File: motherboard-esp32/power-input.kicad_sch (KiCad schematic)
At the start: 8 parts, among them J1 XT60, Q1 MCU60P04-TP, Q2 MCU60P04-TP, SW1 RA1H1C112R

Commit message: boards
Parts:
- removed SW1: RA1H1C112R, bots:SW_RA1H1C112R, symbol bots:RA1H1C112R
- added J2: XT60, bots:XT60_12-14AWG_POWER, symbol bio-robot:XT-60
- added J3: JST_2P_XH, bots:JST_B2B-XH-A_LF__SN_, symbol bio-robot:JST_XH-2
- D1: value SMAZ12-13F -> SMAZ6V8; footprint bots:D_SMB -> bots:D_SMA; symbol bots:D_ZENER_SMAZ12-13F -> bio-robot:D_ZENER_SMAZ6V8; JLC (none) -> DO-214AC(SMA); LCSC C260227 -> C2988335; MPN SMAZ12-13F -> SMAZ6V8; Manufacturer Micro Commercial Co -> EIC Semicon C; Price 0.63 -> 0.1464
- F1: value 0501015.WR1 -> 0437005.WR; symbol bots:Fuse_0501015.WR1 -> bio-robot:Fuse_Littelfuse5A; LCSC C410346 -> C99541; MPN 0501015.WR1 -> 0437005.WR; Price 0.0992 -> 0.1509
- J1: symbol bots:XT-60 -> bio-robot:XT-60
- Q1, Q2: value MCU60P04-TP -> DOD4185; symbol bots:MCU60P04-TP -> bio-robot:Q_Pch40V45A; LCSC C130101 -> C41430591; MPN (none) -> DOD4185
- R1, R2: symbol bots:R_100k -> bio-robot:R_100k
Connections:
- net GND: now also J2.1, J3.2
- net SW: now also J3.1
- net VBAT: now also J2.2
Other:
- note added: "3 cell battery -> 12.6V max, 10.2V min. parallel for modularity"

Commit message: proof of concept
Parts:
- removed F1: 0437005.WR, bots:Fuse_1206_3216Metric, symbol bio-robot:Fuse_Littelfuse5A
- removed J1, J2: XT60, bots:XT60_12-14AWG_POWER, symbol bio-robot:XT-60
- added BT1, BT2, BT3, BT4, BT5, BT6: Keystone_254_BatteryClip_Holder, bio-robot:BAT_254_18650_Holder, symbol bio-robot:Keystone_254_BatteryClip_Holder
- added F2: 0501010.WR1, bio-robot:Fuse_1206_3216Metric, symbol bio-robot:Fuse_0501010.WR1
- D1: footprint bots:D_SMA -> bio-robot:D_SMA
- J3: footprint bots:JST_B2B-XH-A_LF__SN_ -> bio-robot:JST_B2B-XH-A_LF__SN_
- Q1, Q2: footprint bots:DPAK-3_ONS -> bio-robot:DPAK-3_ONS
- R1, R2: footprint bots:R_0603_1608Metric -> bio-robot:R_0603_1608Metric
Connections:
- net FUSE_VCC: now also F2.2
- net GND: now also BT3.P-, BT6.P-
- net VBAT: now also BT1.P+, BT4.P+, F2.1
- new net: BT2.P-, BT3.P+
- new net: BT4.P-, BT5.P+
- new net: BT5.P-, BT6.P+
- new net: BT1.P-, BT2.P+
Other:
- note added: "3 cell battery -> 12.6V max, 10.2V min. parallel for modularity board contact 18650 holders can generally only go up to 3-5A max so 2 in parallel allow up to 10A continous."
- note removed: "3 cell battery -> 12.6V max, 10.2V min. parallel for modularity"

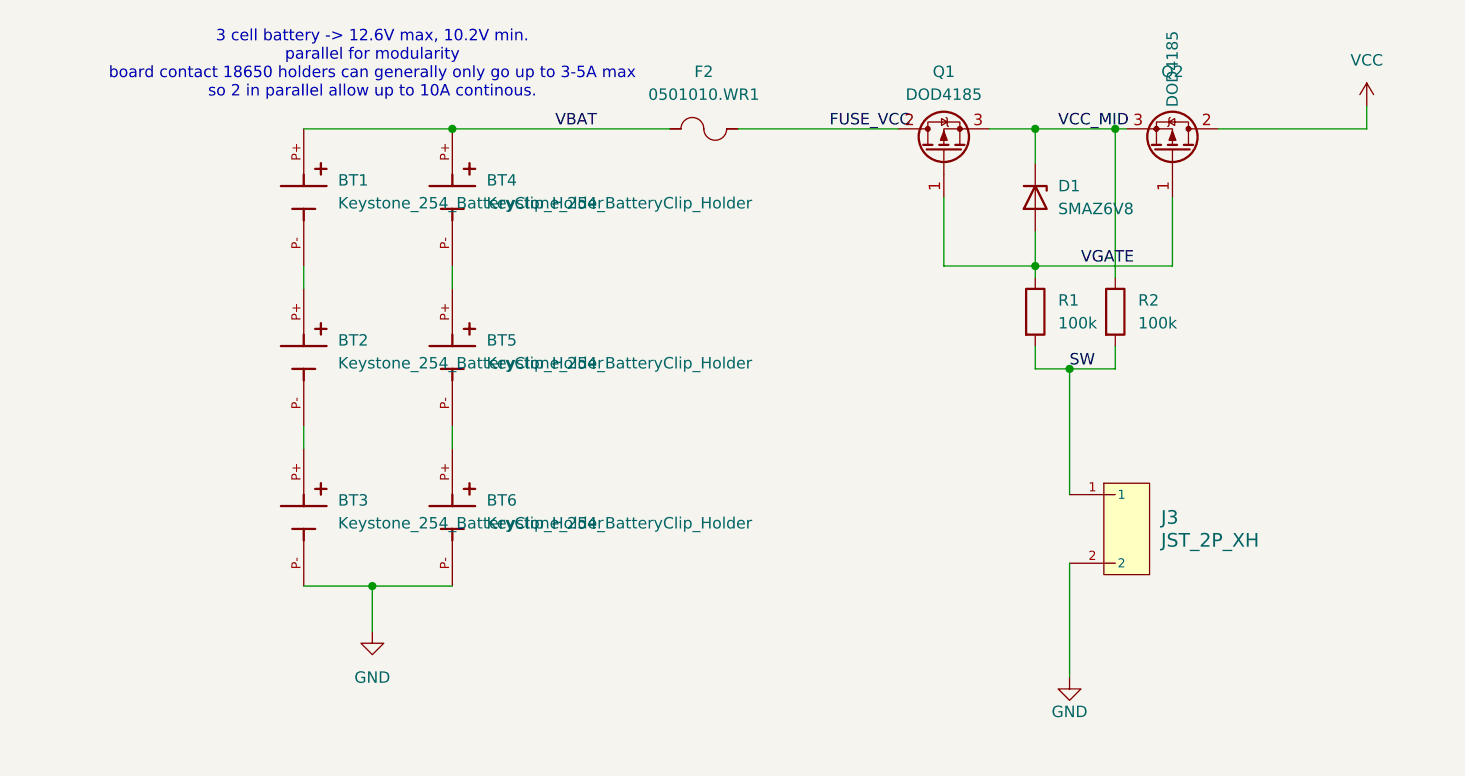
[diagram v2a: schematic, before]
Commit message: split into two boards for dc/dc converter
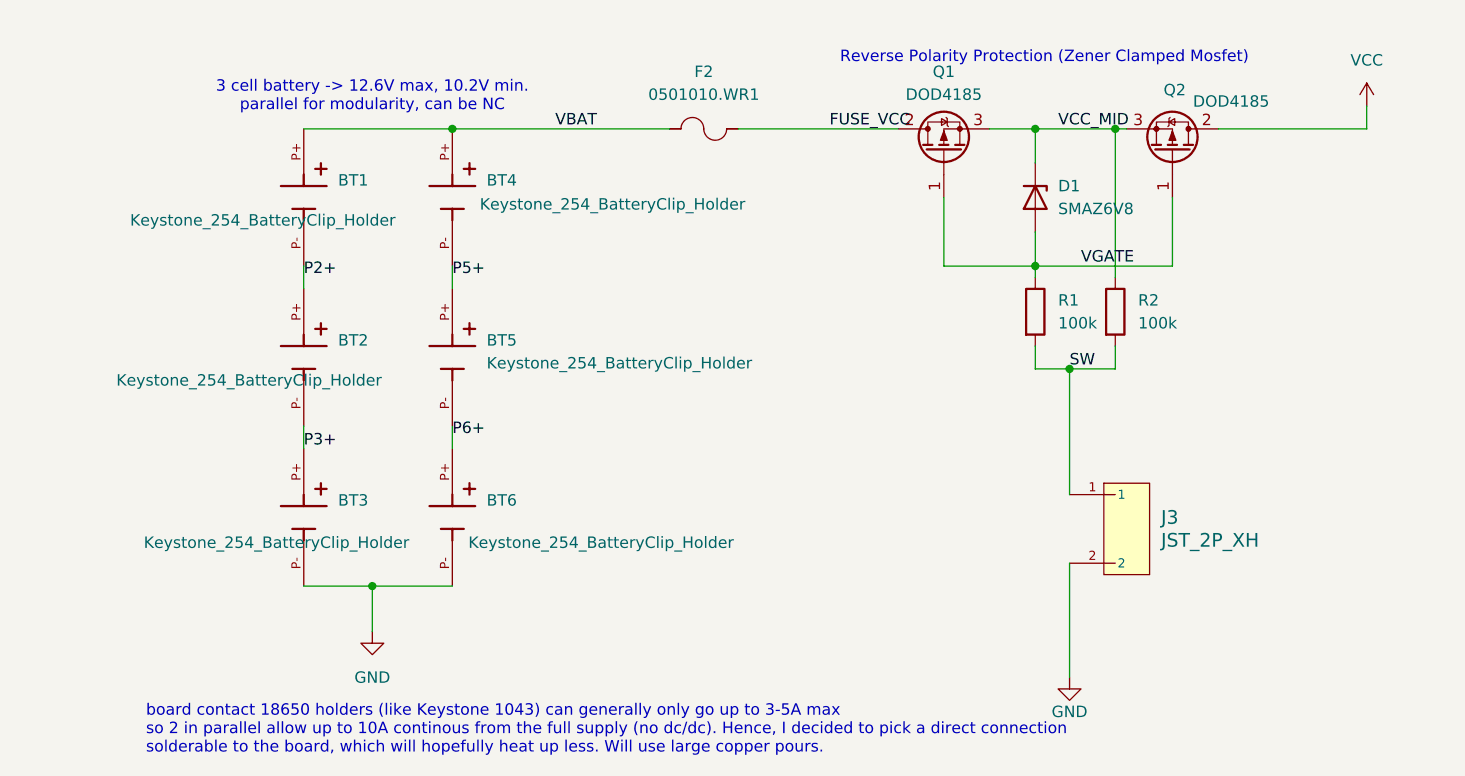
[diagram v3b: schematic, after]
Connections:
- net P3+: now reaches BT2.P-, BT3.P+
- net P5+: now reaches BT4.P-, BT5.P+
- net P6+: now reaches BT5.P-, BT6.P+
- net P2+: now reaches BT1.P-, BT2.P+
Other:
- note added: "3 cell battery -> 12.6V max, 10.2V min. parallel for modularity, can be NC"
- note added: "Reverse Polarity Protection (Zener Clamped Mosfet)"
- note added: "board contact 18650 holders (like Keystone 1043) can generally only go up to 3-5A max so 2 in parallel allow up to 10A continous from the full supply (no dc/dc). Hence, I decided to pick a direct connection solderable to the board, which will hopefully heat up less. Will use large copper pours."
- note removed: "3 cell battery -> 12.6V max, 10.2V min. parallel for modularity board contact 18650 holders can generally only go up to 3-5A max so 2 in parallel allow up to 10A continous."

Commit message: update
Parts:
- removed BT1, BT2, BT3, BT4, BT5, BT6: Keystone_254_BatteryClip_Holder, bio-robot:BAT_254_18650_Holder, symbol bio-robot:Keystone_254_BatteryClip_Holder
- added BT8: Keystone_1048P_DualBatteryHolder, bio-robot:BAT_1048P, symbol bio-robot:Keystone_1048P_DualBatteryHolder
- added D2: SMAZ3V6, bots:D_SMA, symbol bio-robot:D_ZENER_SMAZ3V6
- added F1: 0437005.WR, bio-robot:Fuse_1206_3216Metric, symbol bio-robot:Fuse_0437005.WR
- added J4: JST_2P_XH, bio-robot:JST_B2B-XH-A_LF__SN_, symbol bio-robot:JST_XH-2
- added J7: XT60, bio-robot:AMASS_XT60PW-M, symbol bio-robot:XT-60-RA
- added Q3, Q4: DOD4185, bio-robot:DPAK-3_ONS, symbol bio-robot:Q_Pch40V45A
- added R3, R4: 100k, bio-robot:R_0603_1608Metric, symbol bio-robot:R_100k
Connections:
- net GND: now also BT8.N2, J4.2; no longer J3.2
- net VBAT: now also J7.2
- new net +BATT: Q4.2 (D)
- new net BAT5V_MID: D2.1 (K), Q3.3 (S), Q4.3 (S), R4.1
- new net FUSE_BAT5V: F1.2, Q3.2 (D)
- new net GNDPWR: J3.2, J7.1
- new net SW2: J4.1, R3.2, R4.2
- new net VBAT5V: BT8.P1, F1.1
- new net VBAT5V_P2: BT8.N1, BT8.P2
- new net VGATE_2: D2.2 (A), Q3.1 (G), Q4.1 (G), R3.1
- no-connect marks 0 -> 1
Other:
- note added: "3 cell battery -> 12.6V max, 10.2V min."
- note removed: "3 cell battery -> 12.6V max, 10.2V min. parallel for modularity, can be NC"
- moved on the sheet: D1, F2, J3, Q1, Q2, R1, R2

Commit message: update
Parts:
- D1: footprint bio-robot:D_SMA -> bots:D_SMA
- J3, J4: footprint bio-robot:JST_B2B-XH-A_LF__SN_ -> bots:JST_B2B-XH-A_LF__SN_
- Q1, Q2, Q3, Q4: footprint bio-robot:DPAK-3_ONS -> bots:DPAK-3_ONS
- R1, R2, R3, R4: footprint bio-robot:R_0603_1608Metric -> bots:R_0603_1608Metric
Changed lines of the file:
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@@
 			)
 		)
-		(property "Footprint" "bio-robot:JST_B2B-XH-A_LF__SN_"
+		(property "Footprint" "bots:JST_B2B-XH-A_LF__SN_"
 			(at 116.84 107.95 0)
 			(hide yes)
@@
 			)
 		)
-		(property "Footprint" "bio-robot:R_0603_1608Metric"
+		(property "Footprint" "bots:R_0603_1608Metric"
 			(at 104.902 111.76 90)
 			(hide yes)
@@
 			)
 		)
-		(property "Footprint" "bio-robot:DPAK-3_ONS"
+		(property "Footprint" "bots:DPAK-3_ONS"
 			(at 111.125 89.027 0)
 			(hide yes)
@@
 			)
 		)
-		(property "Footprint" "bio-robot:R_0603_1608Metric"
+		(property "Footprint" "bots:R_0603_1608Metric"
 			(at 121.412 49.53 90)
 			(hide yes)
@@
 			)
 		)
-		(property "Footprint" "bio-robot:D_SMA"
+		(property "Footprint" "bots:D_SMA"
 			(at 123.19 36.83 0)
 			(hide yes)
@@
 			)
 		)
-		(property "Footprint" "bio-robot:R_0603_1608Metric"
+		(property "Footprint" "bots:R_0603_1608Metric"
 			(at 96.012 111.76 90)
 			(hide yes)
@@
 			)
 		)
-		(property "Footprint" "bio-robot:DPAK-3_ONS"
+		(property "Footprint" "bots:DPAK-3_ONS"
 			(at 136.525 26.797 0)
 			(hide yes)
@@
 			)
 		)
-		(property "Footprint" "bio-robot:DPAK-3_ONS"
+		(property "Footprint" "bots:DPAK-3_ONS"
 			(at 114.935 26.797 0)
 			(hide yes)
@@
 			)
 		)
-		(property "Footprint" "bio-robot:DPAK-3_ONS"
+		(property "Footprint" "bots:DPAK-3_ONS"
 			(at 89.535 89.027 0)
 			(hide yes)
@@
 			)
 		)
-		(property "Footprint" "bio-robot:R_0603_1608Metric"
+		(property "Footprint" "bots:R_0603_1608Metric"
 			(at 130.302 49.53 90)
 			(hide yes)
@@
 			)
 		)
-		(property "Footprint" "bio-robot:JST_B2B-XH-A_LF__SN_"
+		(property "Footprint" "bots:JST_B2B-XH-A_LF__SN_"
 			(at 142.24 45.72 0)
 			(hide yes)

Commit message: adding leds
- need to add UVLO
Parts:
- removed Q3, Q4: DOD4185, bots:DPAK-3_ONS, symbol bio-robot:Q_Pch40V45A
- added Q3, Q4: HL3415A, bio-robot:SOT-23, symbol bio-robot:Q_Pch20V5.6A
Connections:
- net +BATT: now also Q4.3 (D)
- net BAT5V_MID: now also Q3.2 (S), Q4.2 (S)
- net FUSE_BAT5V: now also Q3.3 (D)
- net VGATE_2: now also Q3.1 (G), Q4.1 (G)
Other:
- note added: "board contact 18650 holders (like Keystone 1043 / 1048) can generally only go up to 3-5A max"
- note removed: "board contact 18650 holders (like Keystone 1043) can generally only go up to 3-5A max so 2 in parallel allow up to 10A continous from the full supply (no dc/dc). Hence, I decided to pick a direct connection solderable to the board, which will hopefully heat up less. Will use large copper pours."
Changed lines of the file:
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@@
 		)
 	)
-	(text "board contact 18650 holders (like Keystone 1043) can generally only go up to 3-5A max\nso 2 in parallel allow up to 10A continous from the full supply (no dc/dc). Hence, I decided to pick a direct connection\nsolderable to the board, which will hopefully heat up less. Will use large copper pours."
+	(text "board contact 18650 holders (like Keystone 1043 / 1048) can generally only go up to 3-5A max"
 		(exclude_from_sim no)
-		(at 21.082 77.724 0)
+		(at 21.844 79.248 0)
 		(effects
 			(font
@@
 	)
 	(symbol
+		(lib_id "bio-robot:Q_Pch20V5.6A")
+		(at 113.03 93.98 270)
+		(mirror x)
+		(unit 1)
+		(body_style 1)
+		(exclude_from_sim no)
+		(in_bom yes)
+		(on_board yes)
+		(in_pos_files yes)
+		(dnp no)
+		(property "Reference" "Q4"
+			(at 113.03 85.09 90)
+			(show_name no)
+			(do_not_autoplace no)
+			(effects
+				(font
+					(size 1.27 1.27)
+				)
+			)
+		)
+		(property "Value" "HL3415A"
+			(at 113.03 87.63 90)
+			(show_name no)
+			(do_not_autoplace no)
+			(effects
+				(font
+					(size 1.27 1.27)
+				)
+			)
+		)
+		(property "Footprint" "bio-robot:SOT-23"
+			(at 111.125 89.027 0)
+			(hide yes)
+			(show_name no)
+			(do_not_autoplace no)
+			(effects
+				(font
+					(size 1.27 1.27)
+					(italic yes)
+				)
+				(justify left)
+			)
+		)
+		(property "Datasheet" ""
+			(at 113.03 93.98 0)
+			(hide yes)
+			(show_name no)
+			(do_not_autoplace no)
+			(effects
+				(font
+					(size 1.27 1.27)
+				)
+			)
+		)
+		(property "Description" "P-Channel 1.18nF 1.3W 11nC@4.5V 125pF 20V 31mΩ@4.5V、41mΩ@2.5V 5.6A 620mV 88pF P-Channel SOT-23 MOSFETs ROHS"
+			(at 113.03 93.98 0)
+			(hide yes)
+			(show_name no)
+			(do_not_autoplace no)
+			(effects
+				(font
+					(size 1.27 1.27)
+				)
+			)
+		)
+		(property "LCSC" "C28646270"
+			(at 113.03 93.98 0)
+			(hide yes)
+			(show_name no)
+			(do_not_autoplace no)
+			(effects
+				(font
+					(size 1.27 1.27)
+				)
+			)
+		)
+		(property "MPN" "HL3415A"
+			(at 113.03 93.98 0)
+			(hide yes)
+			(show_name no)
+			(do_not_autoplace no)
+			(effects
+				(font
+					(size 1.27 1.27)
+				)
+			)
+		)
+		(property "JLC" "SOT-23"
+			(at 113.03 93.98 0)
+			(hide yes)
+			(show_name no)
+			(do_not_autoplace no)
+			(effects
+				(font
+					(size 1.27 1.27)
+				)
+			)
+		)
+		(pin "1"
+		)
+		(pin "2"
+		)
+		(pin "3"
+		)
+		(instances
+			(project "motherboard-esp32"
+				(path "/d5fb8fba-70d9-4abd-aa21-c96ccdcfa753/d9cb3474-f996-47d2-9ced-ceac8301b71b"
+					(reference "Q4")
+					(unit 1)
+				)
+			)
+		)
+	)
+	(symbol
+		(lib_id "bio-robot:Q_Pch20V5.6A")
+		(at 87.63 93.98 90)
+		(unit 1)
+		(body_style 1)
+		(exclude_from_sim no)
+		(in_bom yes)
+		(on_board yes)
+		(in_pos_files yes)
+		(dnp no)
+		(fields_autoplaced yes)
+		(property "Reference" "Q3"
+			(at 87.63 85.09 90)
+			(show_name no)
+			(do_not_autoplace no)
+			(effects
+				(font
+					(size 1.27 1.27)
+				)
+			)
+		)
+		(property "Value" "HL3415A"
+			(at 87.63 87.63 90)
+			(show_name no)
+			(do_not_autoplace no)
+			(effects
+				(font
+					(size 1.27 1.27)
+				)
+			)
+		)
+		(property "Footprint" "bio-robot:SOT-23"
+			(at 89.535 89.027 0)
+			(hide yes)
+			(show_name no)
+			(do_not_autoplace no)
+			(effects
+				(font
+					(size 1.27 1.27)
+					(italic yes)
+				)
+				(justify left)
+			)
+		)
+		(property "Datasheet" ""
+			(at 87.63 93.98 0)
+			(hide yes)
+			(show_name no)
+			(do_not_autoplace no)
+			(effects
+				(font
+					(size 1.27 1.27)
+				)
+			)
+		)
+		(property "Description" "P-Channel 1.18nF 1.3W 11nC@4.5V 125pF 20V 31mΩ@4.5V、41mΩ@2.5V 5.6A 620mV 88pF P-Channel SOT-23 MOSFETs ROHS"
+			(at 87.63 93.98 0)
+			(hide yes)
+			(show_name no)
+			(do_not_autoplace no)
+			(effects
+				(font
+					(size 1.27 1.27)
+				)
+			)
+		)
+		(property "LCSC" "C28646270"
+			(at 87.63 93.98 0)
+			(hide yes)
+			(show_name no)
+			(do_not_autoplace no)
+			(effects
+				(font
+					(size 1.27 1.27)
+				)
+			)
+		)
+		(property "MPN" "HL3415A"
+			(at 87.63 93.98 0)
+			(hide yes)
+			(show_name no)
+			(do_not_autoplace no)
+			(effects
+				(font
+					(size 1.27 1.27)
+				)
+			)
+		)
+		(property "JLC" "SOT-23"
+			(at 87.63 93.98 0)
+			(hide yes)
+			(show_name no)
+			(do_not_autoplace no)
+			(effects
+				(font
+					(size 1.27 1.27)
+				)
+			)
+		)
+		(pin "1"
+		)
+		(pin "2"
+		)
+		(pin "3"
+		)
+		(instances
+			(project "motherboard-esp32"
+				(path "/d5fb8fba-70d9-4abd-aa21-c96ccdcfa753/d9cb3474-f996-47d2-9ced-ceac8301b71b"
+					(reference "Q3")
+					(unit 1)
+				)
+			)
+		)
+	)
+	(symbol
 		(lib_id "power:GNDPWR")
 		(at 43.18 49.53 0)
@@
 	)
 	(symbol
-		(lib_id "bio-robot:Q_Pch40V45A")
-		(at 113.03 93.98 270)
-		(mirror x)
-		(unit 1)
-		(body_style 1)
-		(exclude_from_sim no)
-		(in_bom yes)
-		(on_board yes)
-		(in_pos_files yes)
-		(dnp no)
-		(property "Reference" "Q4"
-			(at 113.284 87.122 90)
-			(show_name no)
-			(do_not_autoplace no)
-			(effects
-				(font
-					(size 1.27 1.27)
-				)
-			)
-		)
-		(property "Value" "DOD4185"
-			(at 115.316 88.392 90)
-			(show_name no)
-			(do_not_autoplace no)
-			(effects
-				(font
-					(size 1.27 1.27)
-				)
-				(justify left)
-			)
-		)
-		(property "Footprint" "bots:DPAK-3_ONS"
-			(at 111.125 89.027 0)
-			(hide yes)
-			(show_name no)
-			(do_not_autoplace no)
-			(effects
-				(font
-					(size 1.27 1.27)
-					(italic yes)
-				)
-				(justify left)
-			)
-		)
-		(property "Datasheet" "https://jlcpcb.com/api/file/downloadByFileSystemAccessId/8604441185771802624"
-			(at 113.03 93.98 0)
-			(hide yes)
-			(show_name no)
-			(do_not_autoplace no)
-			(effects
-				(font
-					(size 1.27 1.27)
-				)
-			)
-		)
-		(property "Description" "P-Channel 40 V 45A 73.5W Surface Mount D-Pak"
-			(at 113.03 93.98 0)
-			(hide yes)
-			(show_name no)
-			(do_not_autoplace no)
-			(effects
-				(font
-					(size 1.27 1.27)
-				)
-			)
-		)
-		(property "LCSC" "C41430591"
-			(at 113.03 93.98 0)
-			(hide yes)
-			(show_name no)
-			(do_not_autoplace no)
-			(effects
-				(font
-					(size 1.27 1.27)
-				)
-			)
-		)
-		(property "MPN" "DOD4185"
-			(at 113.03 93.98 0)
-			(hide yes)
-			(show_name no)
-			(do_not_autoplace no)
-			(effects
-				(font
-					(size 1.27 1.27)
-				)
-			)
-		)
-		(pin "1"
-		)
-		(pin "2"
-		)
-		(pin "3"
-		)
-		(instances
-			(project "motherboard-esp32"
-				(path "/d5fb8fba-70d9-4abd-aa21-c96ccdcfa753/d9cb3474-f996-47d2-9ced-ceac8301b71b"
-					(reference "Q4")
-					(unit 1)
-				)
-			)
-		)
-	)
-	(symbol
 		(lib_id "bio-robot:Keystone_1048P_DualBatteryHolder")
 		(at 41.91 104.14 90)
@@
 					(unit 1)
 				)
-			)
-		)
-	)
-	(symbol
-		(lib_id "bio-robot:Q_Pch40V45A")
-		(at 87.63 93.98 90)
-		(unit 1)
-		(body_style 1)
-		(exclude_from_sim no)
-		(in_bom yes)
-		(on_board yes)
-		(in_pos_files yes)
-		(dnp no)
-		(fields_autoplaced yes)
-		(property "Reference" "Q3"
-			(at 87.63 85.09 90)
-			(show_name no)
-			(do_not_autoplace no)
-			(effects
-				(font
-					(size 1.27 1.27)
-				)
-			)
-		)
-		(property "Value" "DOD4185"
-			(at 87.63 87.63 90)
-			(show_name no)
-			(do_not_autoplace no)
-			(effects
-				(font
-					(size 1.27 1.27)
-				)
-			)
-		)
-		(property "Footprint" "bots:DPAK-3_ONS"
-			(at 89.535 89.027 0)
-			(hide yes)
-			(show_name no)
-			(do_not_autoplace no)
-			(effects
-				(font
-					(size 1.27 1.27)
-					(italic yes)
-				)
-				(justify left)
-			)
-		)
-		(property "Datasheet" "https://jlcpcb.com/api/file/downloadByFileSystemAccessId/8604441185771802624"
-			(at 87.63 93.98 0)
-			(hide yes)
-			(show_name no)
-			(do_not_autoplace no)
-			(effects
-				(font
-					(size 1.27 1.27)
-				)
-			)
-		)
-		(property "Description" "P-Channel 40 V 45A 73.5W Surface Mount D-Pak"
-			(at 87.63 93.98 0)
-			(hide yes)
-			(show_name no)
-			(do_not_autoplace no)
-			(effects
-				(font
-					(size 1.27 1.27)
-				)
-			)
-		)
-		(property "LCSC" "C41430591"
-			(at 87.63 93.98 0)
-			(hide yes)
-			(show_name no)
-			(do_not_autoplace no)
-			(effects
-				(font
-					(size 1.27 1.27)
-				)
-			)
-		)
-		(property "MPN" "DOD4185"
-			(at 87.63 93.98 0)
-			(hide yes)
-			(show_name no)
-			(do_not_autoplace no)
-			(effects
-				(font
-					(size 1.27 1.27)
-				)
-			)
-		)
-		(pin "1"
-		)
-		(pin "2"
-		)
-		(pin "3"
-		)
-		(instances
-			(project "motherboard-esp32"
-				(path "/d5fb8fba-70d9-4abd-aa21-c96ccdcfa753/d9cb3474-f996-47d2-9ced-ceac8301b71b"
-					(reference "Q3")
-					(unit 1)
-				)
